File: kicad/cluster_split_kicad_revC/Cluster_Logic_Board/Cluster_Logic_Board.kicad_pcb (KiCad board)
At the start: 2 copper layers, 160 x 100 mm, 11 parts, among them J1 POWER_5V, J10 JST_XH_8, J2 OLED_1x4, J3 PIR_LEFT, J4 PIR_CENTER, J5 PIR_RIGHT, SW1 DIPSW_4, U1 HOSYOND_ESP32-S3_N16R8_2x22, U2 DFPLAYER_MINI_1, U3 DFPLAYER_MINI_2

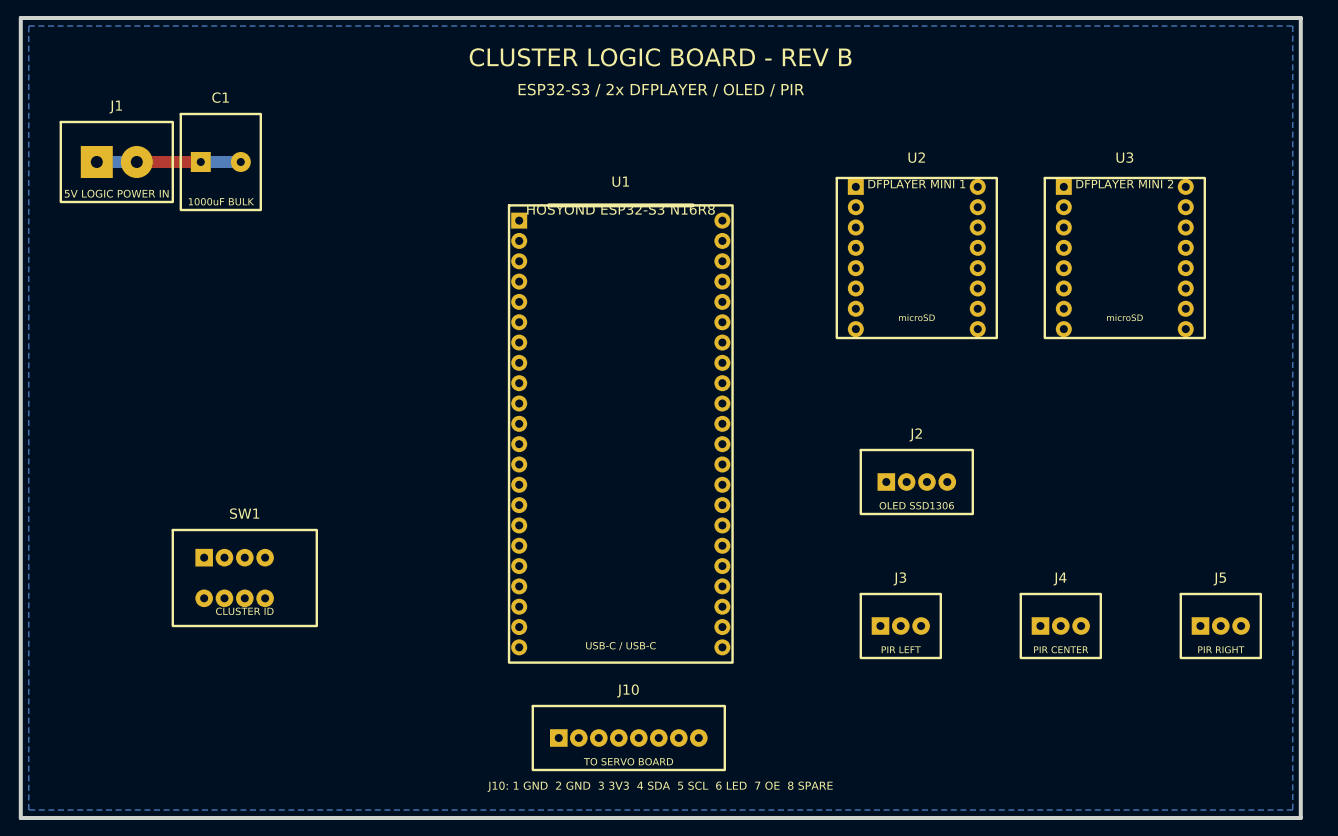
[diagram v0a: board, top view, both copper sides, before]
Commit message: Starting initial version of Controller Logic PCB
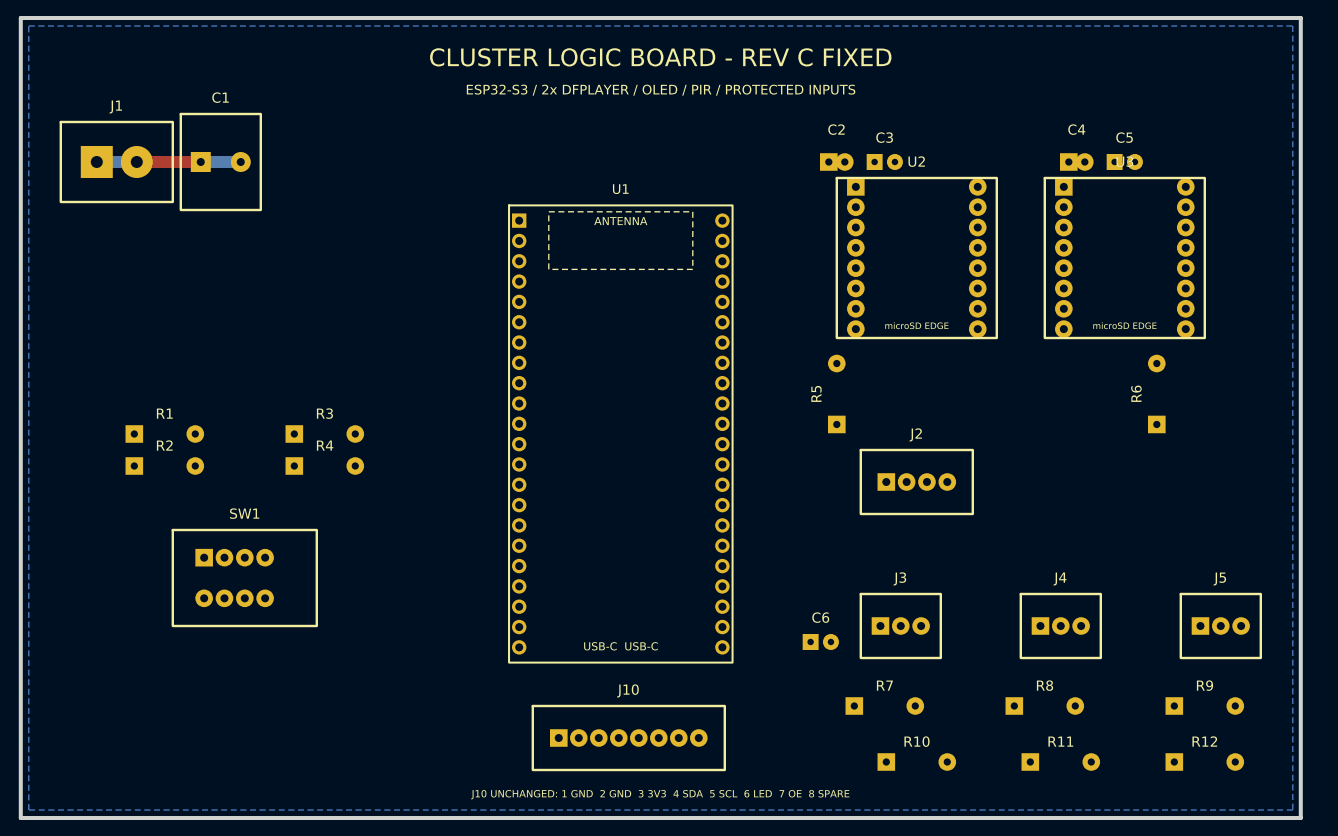
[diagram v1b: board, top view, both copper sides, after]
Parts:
- added C2: 47uF 10V, Custom:C_Radial_47uF, F.Cu at (102.0, 18.0)
- added C3: 100nF, Custom:C_Ceramic_100nF, F.Cu at (108.0, 18.0)
- added C4: 47uF 10V, Custom:C_Radial_47uF, F.Cu at (132.0, 18.0)
- added C5: 100nF, Custom:C_Ceramic_100nF, F.Cu at (138.0, 18.0)
- added C6: 100nF PIR BANK, Custom:C_Ceramic_100nF, F.Cu at (100.0, 78.0)
- added R1: 10k, Custom:R_Axial_10k, F.Cu at (18.0, 52.0)
- added R10: 100k, Custom:R_Axial_100k, F.Cu at (112.0, 93.0)
- added R11: 100k, Custom:R_Axial_100k, F.Cu at (130.0, 93.0)
- added R12: 100k, Custom:R_Axial_100k, F.Cu at (148.0, 93.0)
- added R2: 10k, Custom:R_Axial_10k, F.Cu at (18.0, 56.0)
- added R3: 10k, Custom:R_Axial_10k, F.Cu at (38.0, 52.0)
- added R4: 10k, Custom:R_Axial_10k, F.Cu at (38.0, 56.0)
- added R5: 1k DF1 RX, Custom:R_Axial_1k, F.Cu at (102.0, 47.0)
- added R6: 1k DF2 RX, Custom:R_Axial_1k, F.Cu at (142.0, 47.0)
- added R7: 1k PIR L, Custom:R_Axial_1k, F.Cu at (108.0, 86.0)
- added R8: 1k PIR C, Custom:R_Axial_1k, F.Cu at (128.0, 86.0)
- added R9: 1k PIR R, Custom:R_Axial_1k, F.Cu at (148.0, 86.0)
- U1: value HOSYOND_ESP32-S3_N16R8_2x22 -> Hosyond_ESP32-S3_N16R8_44P; footprint Cluster_Custom:ESP32_S3_HOSYOND_N16R8_2x22_WIDE -> Halloween:Hosyond_ESP32-S3_N16R8_44P
- U2: value DFPLAYER_MINI_1 -> WWZMDiB DFPlayer Mini; footprint Cluster_Custom:DFPlayer_Mini_16P_20x20mm -> Halloween:DFPlayer_Mini_16P
- U3: value DFPLAYER_MINI_2 -> WWZMDiB DFPlayer Mini; footprint Cluster_Custom:DFPlayer_Mini_16P_20x20mm -> Halloween:DFPlayer_Mini_16P
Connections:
- J3 pad 2: PIR_LEFT -> PIR_LEFT_CONN
- J4 pad 2: PIR_CENTER -> PIR_CENTER_CONN
- J5 pad 2: PIR_RIGHT -> PIR_RIGHT_CONN
- U1 pad 11: DF2_RX -> DF2_RX_ESP
- U1 pad 9: DF1_RX -> DF1_RX_ESP
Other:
- board text added: "CLUSTER LOGIC BOARD - REV C FIXED"
- board text added: "ESP32-S3 / 2x DFPLAYER / OLED / PIR / PROTECTED INPUTS"
- board text added: "J10 UNCHANGED: 1 GND 2 GND 3 3V3 4 SDA 5 SCL 6 LED 7 OE 8 SPARE"
- board text removed: "CLUSTER LOGIC BOARD - REV B"
- board text removed: "ESP32-S3 / 2x DFPLAYER / OLED / PIR"
- board text removed: "J10: 1 GND 2 GND 3 3V3 4 SDA 5 SCL 6 LED 7 OE 8 SPARE"

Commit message: Anotther initial starting version of Controller Logic PCB
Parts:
- added C7: 47uF 10V ESP32, Custom:C_Radial_47uF, F.Cu at (51.4, 9.50)
- added C8: 100nF ESP32, Custom:C_Ceramic_100nF, F.Cu at (55.4, 18.5)
- moved U1 11.9 mm to (75.7, 40.2)
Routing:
- net +5V_LOGIC: track 8.00 -> 31.0 mm
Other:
- board text added: "ANTENNA DO NOT BLOCK"
- board text added: "CLUSTER LOGIC BOARD - REV E"
- board text removed: "CLUSTER LOGIC BOARD - REV C FIXED"

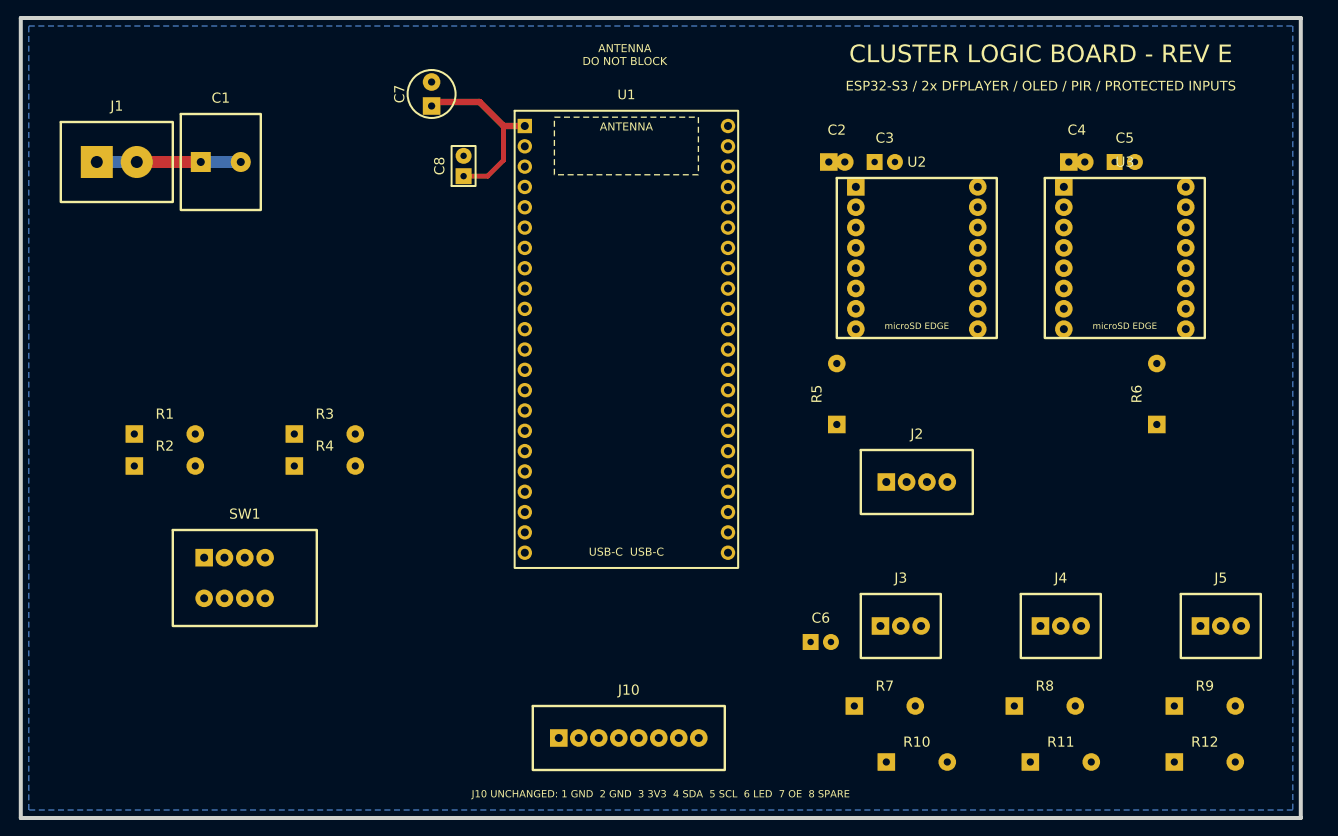
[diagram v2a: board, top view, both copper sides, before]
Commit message: YET Anotther initial starting version of Controller Logic PCB
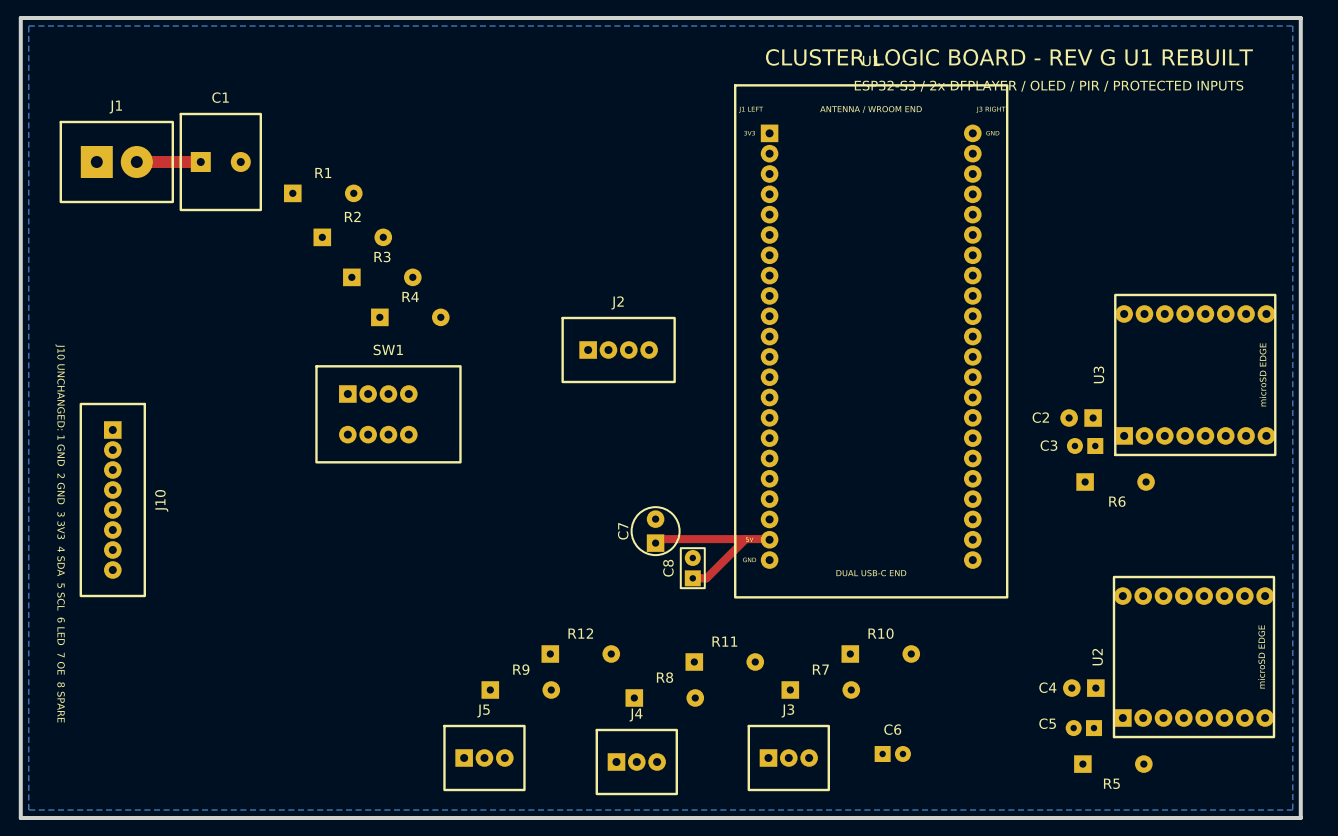
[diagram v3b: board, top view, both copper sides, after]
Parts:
- U1: value Hosyond_ESP32-S3_N16R8_44P -> Hosyond ESP32-S3 N16R8 44-pin DevKit
- moved J5 93.5 mm to (58.0, 92.5)
- moved R9 85.5 mm to (62.5, 84.0)
- moved R12 79.2 mm to (70.0, 79.5)
- moved J10 71.0 mm to (11.5, 60.2), turned to -90 degrees
- moved C5 70.9 mm to (132.9, 88.8), turned to 180 degrees
- moved C4 65.8 mm to (132.9, 83.8), turned to 180 degrees
- moved C7 61.4 mm to (79.3, 64.1)
- moved U2 60.7 mm to (146.7, 79.9), turned to 90 degrees
- moved C8 57.9 mm to (84.0, 68.8)
- moved R5 57.8 mm to (136.6, 93.3), turned to 0 degrees
- moved J4 55.7 mm to (77.0, 93.0)
- moved R8 47.5 mm to (80.5, 85.0)
- moved C2 44.2 mm to (132.5, 50.0), turned to 180 degrees
- moved R11 43.8 mm to (88.0, 80.5)
- moved C3 43.4 mm to (133.0, 53.5), turned to 180 degrees
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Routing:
- net GND: track 18.0 -> 0.00 mm
- net +5V_LOGIC: track 31.0 -> 32.1 mm
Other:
- board text added: "CLUSTER LOGIC BOARD - REV G U1 REBUILT"
- board text removed: "ANTENNA DO NOT BLOCK"
- board text removed: "CLUSTER LOGIC BOARD - REV E"

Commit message: REV G version of Controller Logic PCB - might be ready for first attempt at fab
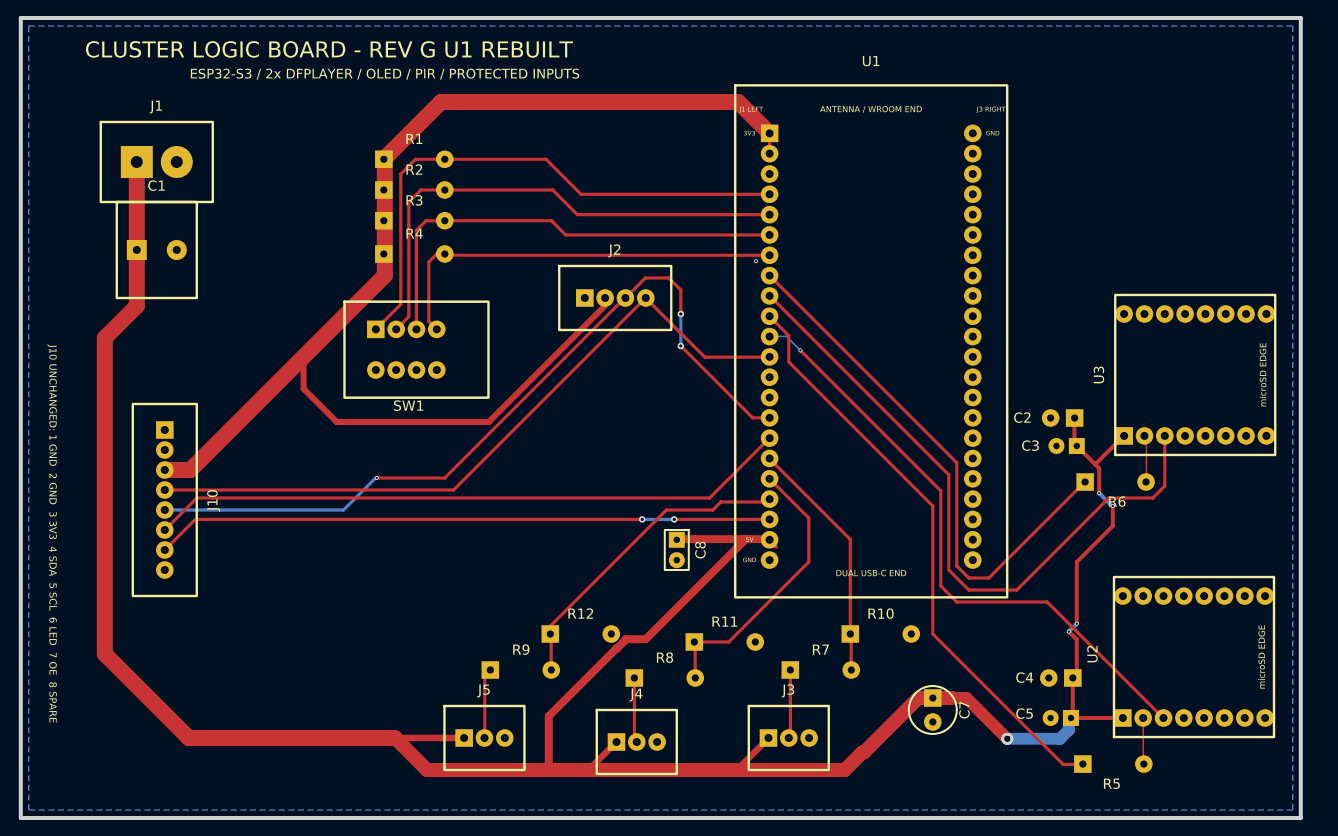
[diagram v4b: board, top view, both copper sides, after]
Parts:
- removed C6: 100nF PIR BANK, Custom:C_Ceramic_100nF
- moved C7 41.2 mm to (114.0, 86.5), turned to -90 degrees
- moved C1 13.6 mm to (17.0, 29.0)
- moved R1 12.2 mm to (49.2, 17.7)
- moved R2 9.70 mm to (49.2, 21.5)
- moved SW1 8.81 mm to (49.5, 41.5)
- moved R3 8.13 mm to (49.2, 25.3)
- moved R4 7.94 mm to (49.2, 29.5)
- moved J2 6.51 mm to (74.3, 35.0)
- moved J10 6.50 mm to (18.0, 60.2)
- moved J1 5.00 mm to (17.0, 18.0)
- moved C4 3.14 mm to (130.0, 82.5)
- moved C5 3.14 mm to (130.0, 87.5)
- moved C8 3.03 mm to (82.0, 66.5), turned to -90 degrees
- moved J3 2.50 mm to (96.0, 90.0)
- moved J4 2.50 mm to (77.0, 90.5)
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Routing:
- net +5V_LOGIC: track 32.1 -> 326.6 mm, vias 0 -> 5
- net +3V3_LOGIC: track 0.00 -> 158.9 mm, vias 0 -> 1
- net I2C_SCL: track 0.00 -> 99.0 mm, vias 0 -> 3
- net I2C_SDA: track 0.00 -> 88.6 mm
- net DF2_TX: track 0.00 -> 83.3 mm
- net LED_DATA_3V3: track 0.00 -> 80.4 mm
- net PCA_OE_N: track 0.00 -> 77.2 mm, vias 0 -> 2
- net DF1_TX: track 0.00 -> 75.9 mm, vias 0 -> 1
- net DF1_RX_ESP: track 0.00 -> 73.7 mm
- net ID0: track 0.00 -> 69.4 mm
- net DF2_RX_ESP: track 0.00 -> 67.6 mm
- net ID1: track 0.00 -> 63.6 mm
- net ID2: track 0.00 -> 57.8 mm
- net ID3: track 0.00 -> 51.9 mm
- net PIR_RIGHT: track 0.00 -> 39.4 mm
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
